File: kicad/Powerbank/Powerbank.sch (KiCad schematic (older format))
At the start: 8 parts

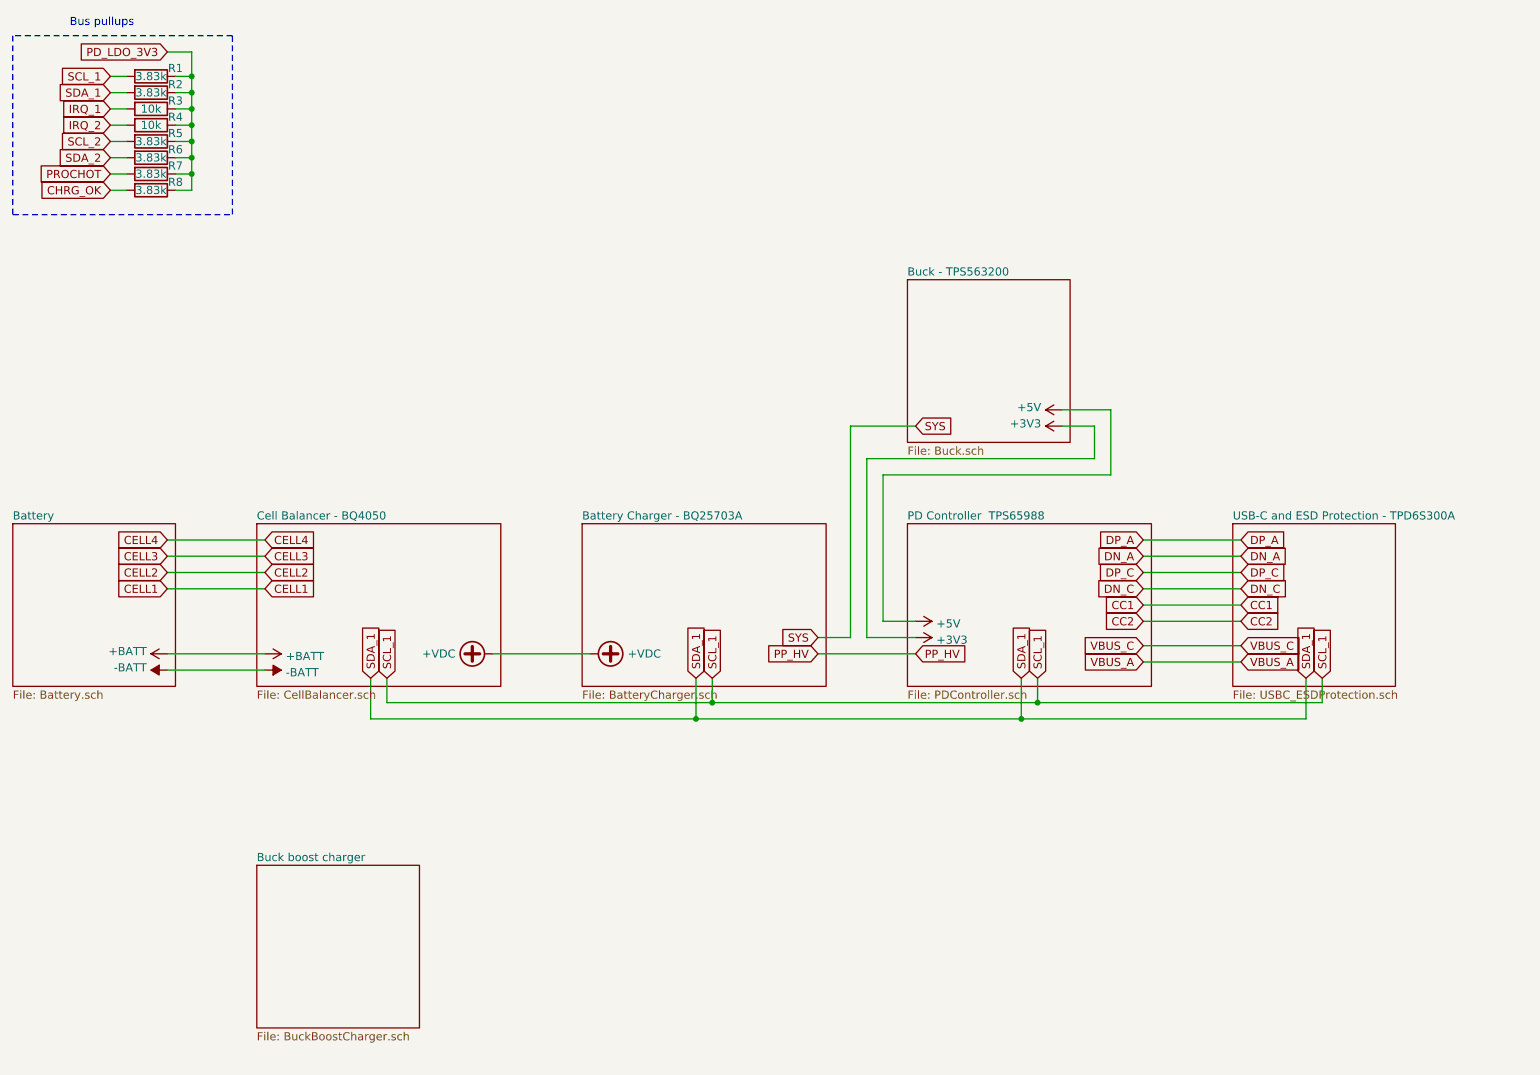
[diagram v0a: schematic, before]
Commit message: Add processor and PD controller
Just trying to create a first schematic over the pieces in the project.
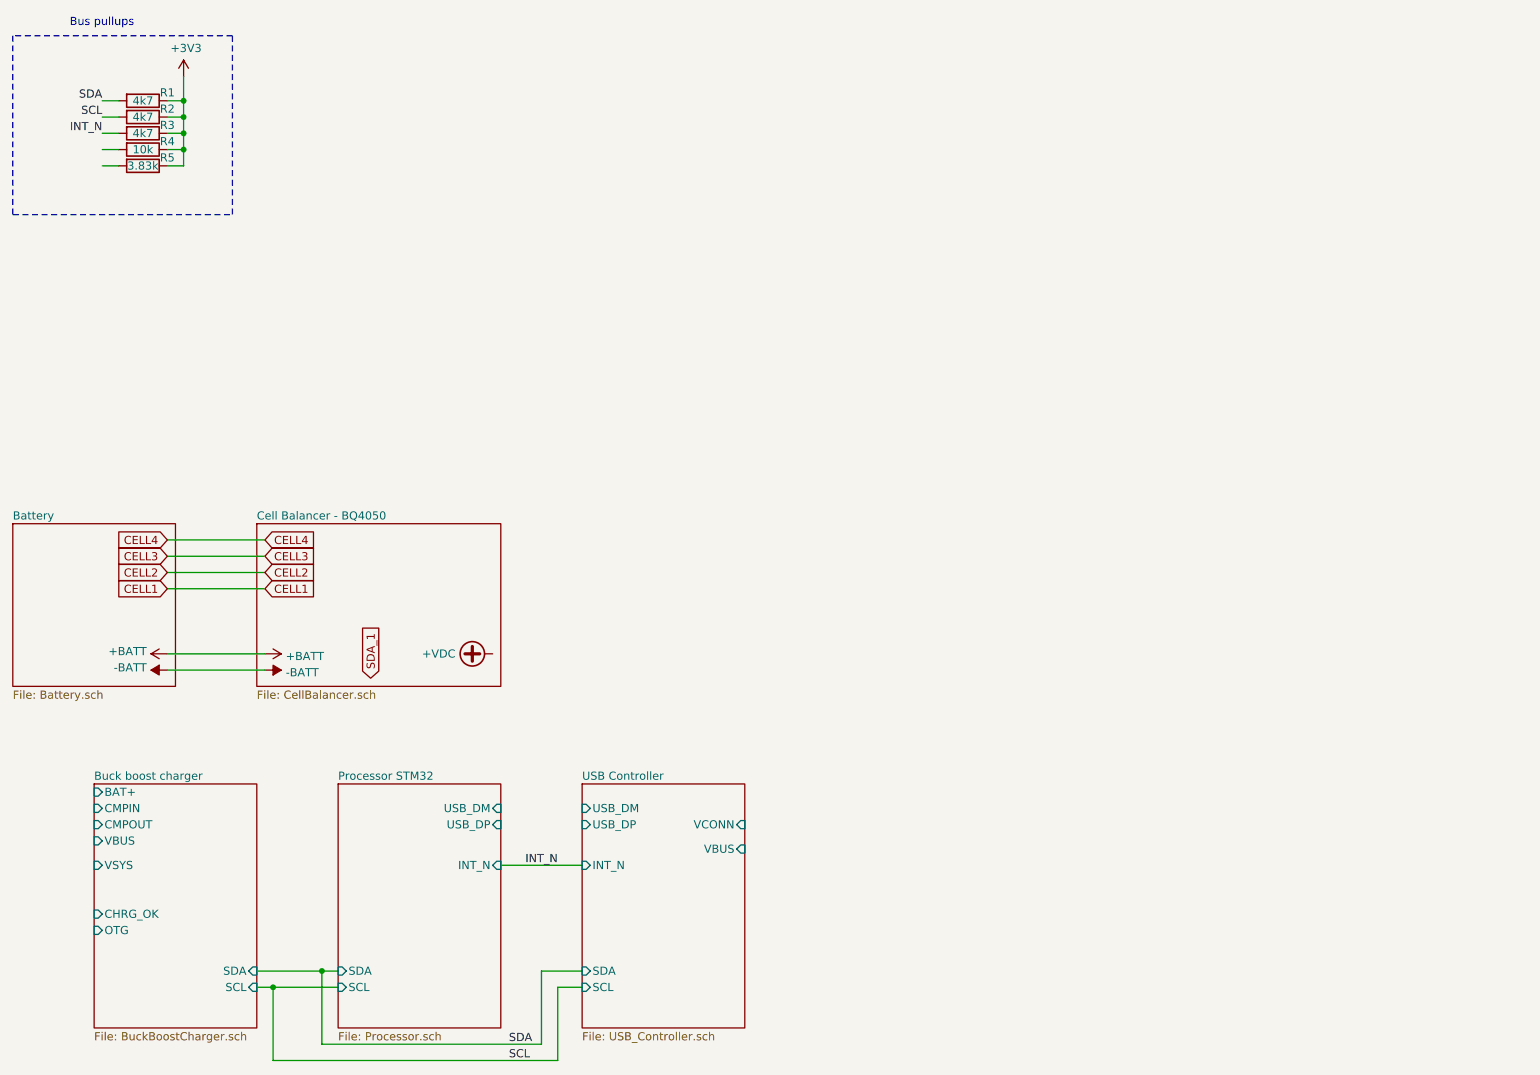
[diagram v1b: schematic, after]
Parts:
- removed R6, R7, R8: 3.83k, Resistor_SMD:R_0603_1608Metric, symbol Device:R
- R1, R2: value 3.83k -> 4k7
- R3: value 10k -> 4k7
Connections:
- net labels added: INT_N, SCL, SDA
- net labels removed: +5V, CC1, CC2, CHRG_OK, DN_A, DN_C, DP_A, DP_C, IRQ_1, IRQ_2, PD_LDO_3V3, PP_HV, PROCHOT, SCL_1, SCL_2, SDA_2, SYS, VBUS_A, VBUS_C
- wire segments 68 -> 34
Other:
- moved on the sheet: R1, R2, R3, R4, R5
